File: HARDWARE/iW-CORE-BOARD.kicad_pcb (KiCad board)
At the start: 4 copper layers, 118 x 80 mm, 120 parts, among them J1 Conn_01x40_MountingPin, J2 Conn_01x06_MountingPin, J3 1746142-1, J4 Conn_02x09_Counter_Clockwise, J5 Conn_02x09_Counter_Clockwise, J7 USB_C_Receptacle_USB2.0, J8 Conn_02x05_Odd_Even, J9 USB_C_Receptacle_USB2.0, P1 ST-TF-003A, SW1 SW_Push, SW2 SW_Push, SW3 SW_Push, U1 STM32H750VBTx, U10 USBLC6-2SC6, U11 USBLC6-2SC6, U12 LT3465, U2 IP5306, U3 STM32F072CBT6, U7 W25Q256JVS, U9 AMS1117-3.3, Y1 8MHz, Y2 32.768KHz

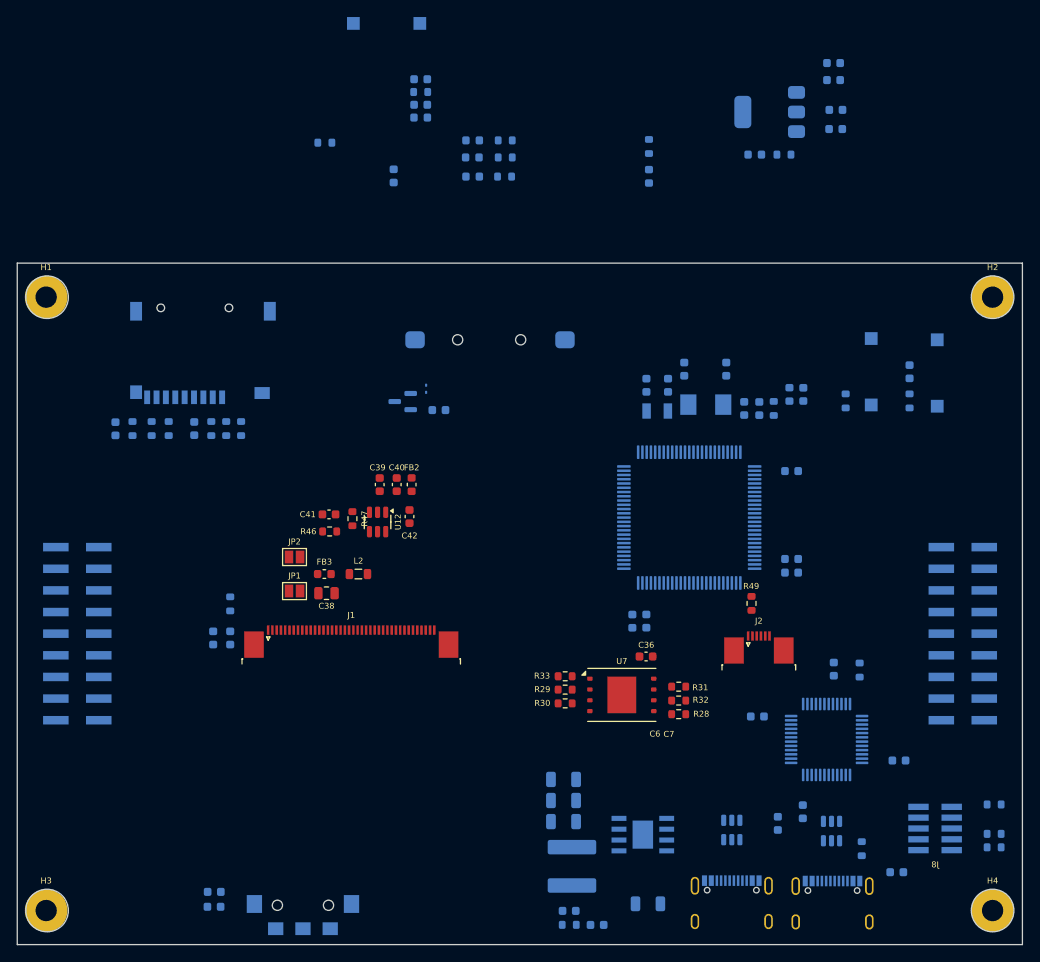
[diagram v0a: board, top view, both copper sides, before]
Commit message: fix fpc
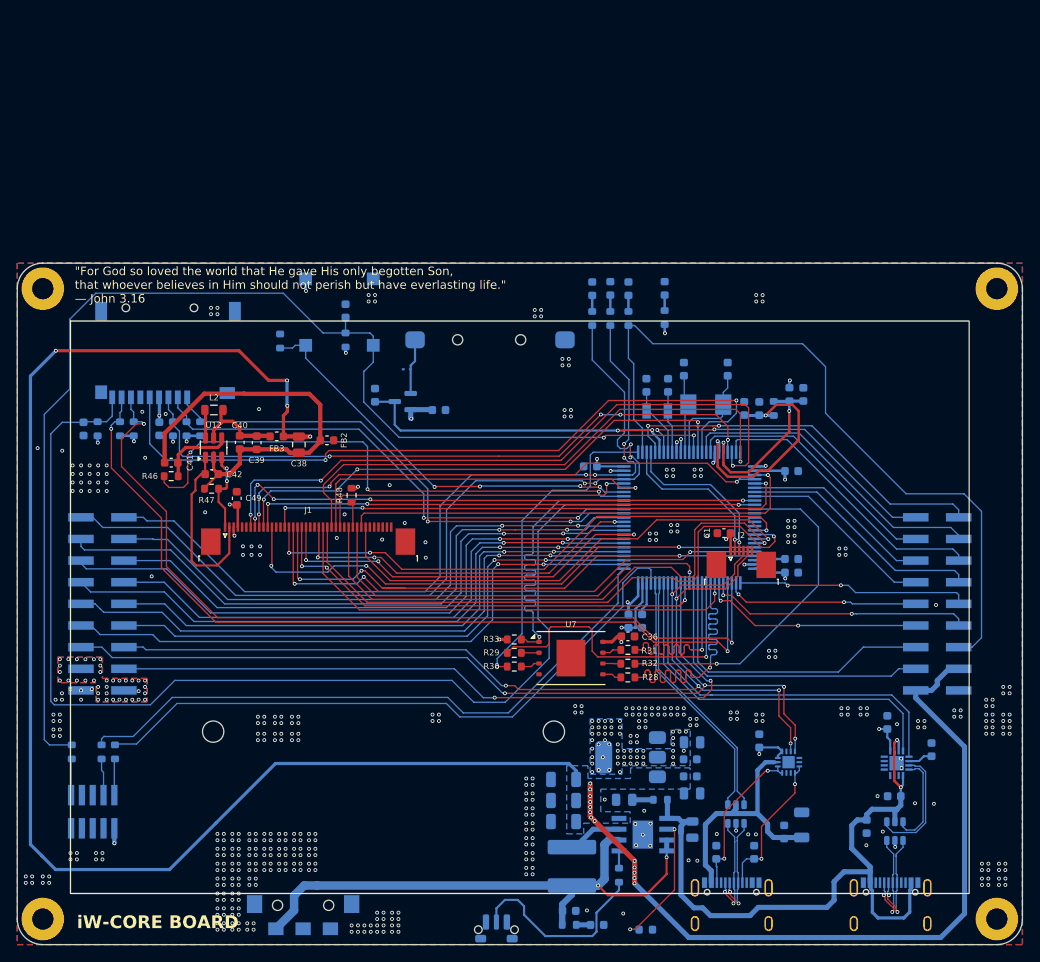
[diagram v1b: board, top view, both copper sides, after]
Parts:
- removed C33, C34, C35, C51, C52: 0.1uF, Capacitor_SMD:C_0603_1608Metric
- removed C50: 100nF, Capacitor_SMD:C_0603_1608Metric
- removed J9: USB_C_Receptacle_USB2.0, Connector_USB:USB_C_Receptacle_G-Switch_GT-USB-7010ASV
- removed JP1, JP2: SolderJumper_2_Open, Jumper:SolderJumper-2_P1.3mm_Open_Pad1.0x1.5mm
- removed R38: 0R, Resistor_SMD:R_1206_3216Metric
- removed R40: 100R, Resistor_SMD:R_0603_1608Metric
- removed R49: 10k, Resistor_SMD:R_0603_1608Metric
- removed R50, R51: 220R, Resistor_SMD:R_0603_1608Metric
- removed U10, U11: USBLC6-2SC6, Package_TO_SOT_SMD:SOT-23-6
- removed U3: STM32F072CBT6, Package_QFP:LQFP-48_7x7mm_P0.5mm
- added C24: 100nF, Capacitor_SMD:C_0603_1608Metric, B.Cu at (185.2, 126.1)
- added C25: 100nF, Capacitor_SMD:C_0603_1608Metric, B.Cu at (188.4, 122.6)
- added C26: 100nF, Capacitor_SMD:C_0603_1608Metric, B.Cu at (187.6, 113.9)
- added C27: 100nF, Capacitor_SMD:C_0603_1608Metric, B.Cu at (192.8, 117.1)
- added C28: 0.1uF, Capacitor_SMD:C_0603_1608Metric, B.Cu at (172.6, 116.1)
- added C29: 0.1uF, Capacitor_SMD:C_0603_1608Metric, B.Cu at (175.5, 126.8)
- added C30: 10uF, Capacitor_SMD:C_1206_3216Metric, B.Cu at (177.6, 126.0)
- added C31: 470pF, Capacitor_SMD:C_0603_1608Metric, B.Cu at (172.0, 129.2)
- added D2: USBLC6-2SC6, PCM_Package_TO_SOT_SMD_AKL:SOT-23-6, B.Cu at (169.9, 124.7)
- added G***: LOGO, LOGO, B.Cu at (190.2, 69.2)
- added H5: MountingHole, MountingHole:MountingHole_2.5mm, F.Cu at (148.5, 115.0)
- added H6: MountingHole, MountingHole:MountingHole_2.5mm, F.Cu at (108.5, 115.0)
- added J6: USB_C_Receptacle_USB2.0, Connector_USB:USB_C_Receptacle_G-Switch_GT-USB-7010ASV, B.Cu at (188.0, 136.5)
- added REF**: display-4.3, Display-Rep:display-4.3, F.Cu at (91.8, 134.0)
- added U4: CH343P, CH343P:QFN50P300X300X80-17N, B.Cu at (188.7, 118.7)
- added U5: FUSB302B01MPX, Package_DFN_QFN:WQFN-14-1EP_2.5x2.5mm_P0.5mm_EP1.45x1.45mm, B.Cu at (176.1, 118.6)
- C1, C49, R48: moved to F.Cu
- C17, C18, C44, C46: footprint Capacitor_SMD:C_0603_1608Metric -> Capacitor_SMD:C_0805_2012Metric
- C32: value 0.1uF -> 470pF
- D4: value LED -> USBLC6-2SC6; footprint LED_SMD:LED_0603_1608Metric -> PCM_Package_TO_SOT_SMD_AKL:SOT-23-6
- SW3: footprint Button_Switch_SMD:SW_SPST_CK_RS282G05A3 -> Button_Switch_SMD:SW_Push_1P1T-MP_NO_Horizontal_Alps_SKRTLAE010
- moved R44 108.5 mm to (91.9, 117.4), turned to -90 degrees
- moved SW3 107.2 mm to (141.8, 138.2)
- moved R42 105.2 mm to (95.4, 117.4), turned to -90 degrees
- moved R41 103.8 mm to (97.0, 117.4), turned to -90 degrees
- moved D1 98.9 mm to (159.3, 138.2)
- moved J8 98.9 mm to (94.4, 124.4), turned to 90 degrees
- moved C18 93.7 mm to (164.8, 126.5), turned to -90 degrees
- moved R11 92.7 mm to (156.1, 131.8), turned to -90 degrees
- moved R9 87.7 mm to (161.0, 123.0), turned to 180 degrees
- moved C17 85.0 mm to (156.8, 123.0), turned to 180 degrees
- moved D4 82.1 mm to (188.5, 126.7), turned to 90 degrees
- moved C45 81.5 mm to (164.5, 118.2)
- moved C46 81.5 mm to (164.7, 116.2)
- moved C43 80.1 mm to (164.5, 120.2)
- moved C44 79.8 mm to (164.7, 122.2)
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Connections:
- net Net-(J7-VBUS-PadA4) renamed +5V_SW
- C18 pad 1: +5VBUS -> +5V_SERIAL
- C32 pad 1: +5VBUS -> GND
- C32 pad 2: GND -> /MCU/CC2
- C38 pad 1: Net-(JP1-B) -> +5V
- C49 pad 1: +3V3 -> +3.3V
- D4 pad 1: Net-(D4-K) -> /USB-SERIAL/USB_N
- D4 pad 2: +3.3V -> GND
- FB3 pad 1: Net-(JP1-B) -> +5V
- J1 pad 4: +3V3 -> +3.3V
- J2 pad 1: 3.3V -> +3.3V
- J2 pad MP: unconnected-(J2-MountPin-PadMP) -> GND
- J4 pad 10: +3.3V -> PC12
- J4 pad 11: +3.3V -> PA15
- J4 pad 12: PD15 -> PC10
- J4 pad 13: PD14 -> I2C3_SDA
- J4 pad 14: PD9 -> I2C3_SCL
- J4 pad 15: PD8 -> +3.3V
- J4 pad 16: PD7 -> PC8
- J4 pad 17: PD5 -> GND
- J4 pad 18: PD4 -> +3.3V
- J4 pad 3: PE3 -> PD5
- J4 pad 4: PE4 -> PD7
- J4 pad 5: PE5 -> PD2
- J4 pad 6: PE6 -> PD4
- J4 pad 9: PD2 -> PC11
- J5 pad 1: PA2 -> GND
- J5 pad 10: GND -> PE4
- J5 pad 11: GND -> PC4
- J5 pad 12: GND -> PC5
- J5 pad 13: GND -> PA2
- J5 pad 14: PC13 -> PA7
- J5 pad 15: PC12 -> PC2
- J5 pad 16: PC11 -> PC3
- J5 pad 17: PC10 -> PE6
- J5 pad 18: PC8 -> PC13
- J5 pad 2: PA7 -> +5V
- J5 pad 3: PA9 -> +5V
- J5 pad 4: PA10 -> PD15
- J5 pad 5: PA15 -> PE3
- J5 pad 6: PC2 -> PD14
- J5 pad 7: PC3 -> PD8
- J5 pad 8: PC4 -> PD9
- J5 pad 9: PC5 -> PE5
- J7 pad A5: unconnected-(J7-CC1-PadA5) -> /MCU/CC1
- J7 pad B5: unconnected-(J7-CC2-PadB5) -> /MCU/CC2
- R41 pad 1: SWDIO_OB -> SWDIO
- R42 pad 1: SWDCLK_OB -> SWDCLK
- R44 pad 1: NRST_OB -> NRST
- R48 pad 2: +3V3 -> +3.3V
- R9 pad 1: +5VBUS -> +5V_SERIAL
- U1 pad 3: PE4 -> TP_RST
- U1 pad 4: PE5 -> TP_INT
- U1 pad 51: TP_RST -> PE5
- U1 pad 52: TP_INT -> PE4
- U1 pad 68: PA9 -> USART1_TX
- U1 pad 69: PA10 -> USART1_RX
- U2 pad 1: +5VBUS -> +5V_SERIAL
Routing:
- net +5V: track 0.00 -> 263.5 mm, vias 0 -> 17
- net NRST: track 0.00 -> 145.7 mm, vias 0 -> 2
- net SD_DET: track 0.00 -> 131.5 mm
- net I2C3_SDA: track 0.00 -> 118.8 mm, vias 0 -> 5
- net I2C3_SCL: track 0.00 -> 112.0 mm, vias 0 -> 5
- net PE0: track 0.00 -> 102.5 mm, vias 0 -> 4
- net SDMMC2_D0: track 0.00 -> 102.0 mm, vias 0 -> 2
- net SDMMC2_D1: track 0.00 -> 101.8 mm, vias 0 -> 2
- net PE1: track 0.00 -> 93.6 mm, vias 0 -> 4
- net SDMMC2_CK: track 0.00 -> 87.5 mm, vias 0 -> 2
- net PE3: track 0.00 -> 87.2 mm
- net PC8: track 0.00 -> 85.1 mm, vias 0 -> 2
- net +5V_SERIAL: track 0.00 -> 80.3 mm, vias 0 -> 2
- net LTDC_R2: track 0.00 -> 77.7 mm, vias 0 -> 3
- net SDMMC2_CMD: track 0.00 -> 77.3 mm, vias 0 -> 4
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- added copper zone on B.Cu, net +3.3V
- added copper zone on F.Cu, net +3.3V
- added copper zone on In2.Cu, net +3.3V
- added copper zone on B.Cu, net +5V
- added copper zone on B.Cu, net GND
- added copper zone on F.Cu, net GND
- added copper zone on In1.Cu, net GND
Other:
- outline, holes or cut-outs redrawn
- board text added: "+3.3"
- board text added: "+5"
- board text added: "BATTERY BL-5C"
- board text added: "BOOT"
- board text added: "GND"
- board text added: "ON"
- board text added: "PA10"
- board text added: "PA15"
- board text added: "PA2"
- board text added: "PA7"
- board text added: "PA9"
- board text added: "PC10"
- board text added: "PC11"
- board text added: "PC12"
- board text added: "PC13"
- board text added: "PC2"
- board text added: "PC3"
- board text added: "PC4"
- board text added: "PC5"
- board text added: "PC8"
- board text added: "PD0"
- board text added: "PD1"
- board text added: "PD14"
- board text added: "PD2"
- board text added: "PD4"
- board text added: "PD5"
- board text added: "PD7"
- board text added: "PD8"
- board text added: "PD9"
- board text added: "PE0"
- board text added: "PE1"
- board text added: "PE3"
- board text added: "PE4"
- board text added: "PE5"
- board text added: "PE6"
- board text added: "RST"
- board text added: "SWD"
- board text added: "USB-OTG"
- board text added: "USB-SERIAL"
- board text added: "iW-CORE BOARD"
- board text added: "{dblquote}For God so loved the world that He gave His only begotten Son, that whoever believes in Him should not perish but have everlasting life.{dblquote} — John 3.16"
